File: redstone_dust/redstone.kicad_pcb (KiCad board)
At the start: 2 copper layers, 40 x 40 mm, 73 parts, among them J1 1x4_Pogo, J2 1x4_Pogo, J3 1x4_Pogo, J4 1x4_Pogo, J5 1x4_Pogo, J6 1x4_Pogo, J7 1x4_Pogo, J8 1x4_Pogo, J9 2.54mm_ProgrammingPin, Q1 BC108, Q2 BC108, Q3 BC108, Q4 BC108, SW1 SW_Push_Open, U1 RP2040, U2 RBT05W24S05, U3 TPS62162DSG, U5 W25Q16JVSS

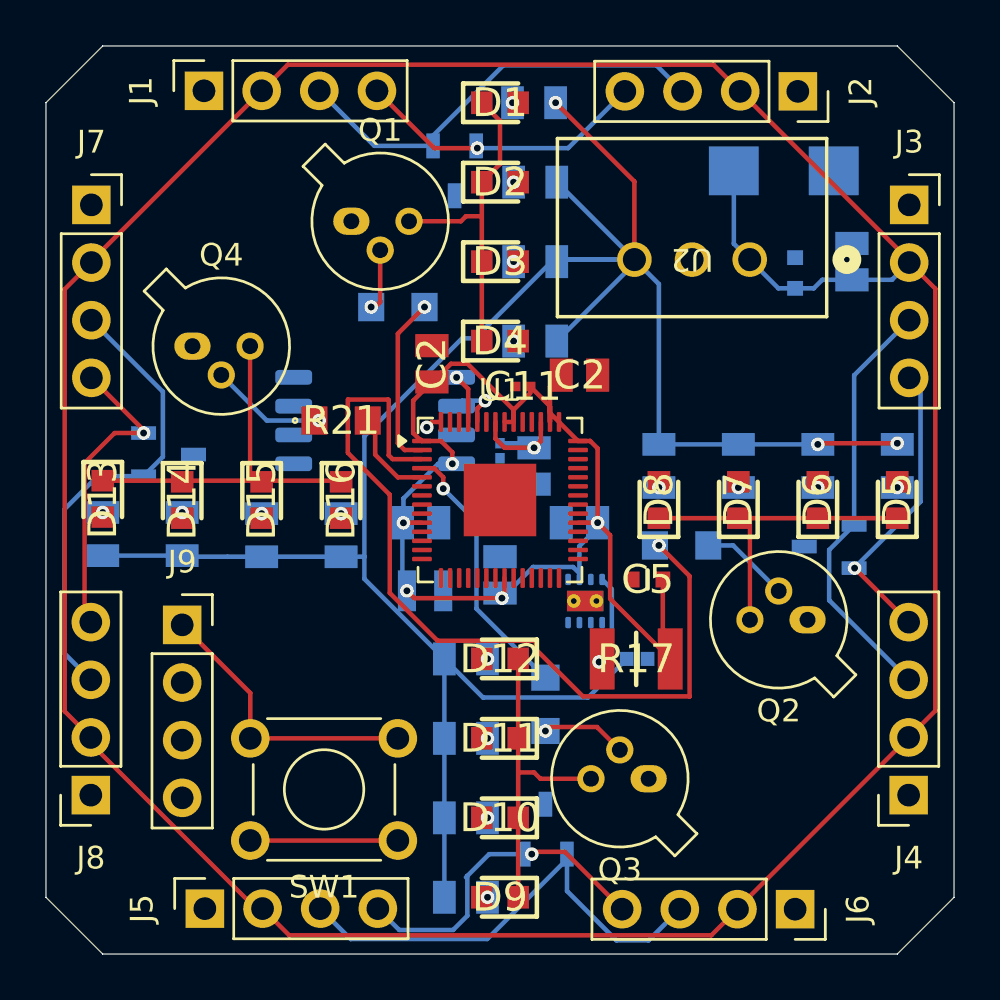
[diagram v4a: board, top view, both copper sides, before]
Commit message: remove all traces to restart layout
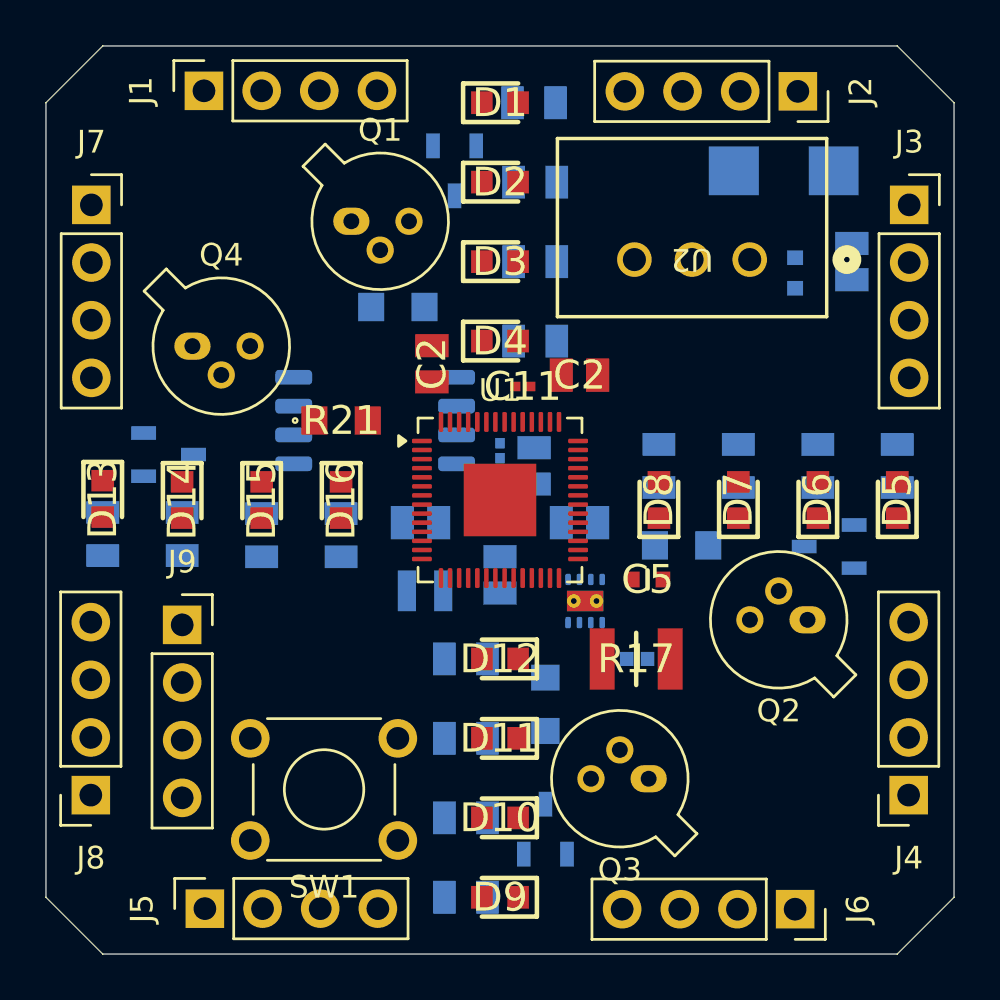
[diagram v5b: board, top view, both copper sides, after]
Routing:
- net VCC: track 142.7 -> 0.00 mm
- net /5V_LOCAL: track 98.8 -> 0.00 mm, vias 3 -> 0
- net /3.3V_LOCAL: track 62.5 -> 0.00 mm, vias 5 -> 0
- net Net-(U1-GPIO1): track 37.8 -> 0.00 mm, vias 1 -> 0
- net /S_TX: track 21.2 -> 0.00 mm
- net /W_TX: track 20.6 -> 0.00 mm
- net /N_TX: track 19.2 -> 0.00 mm
- net /E_TX: track 18.7 -> 0.00 mm
- net Net-(D13-K): track 16.5 -> 0.00 mm
- net Net-(D5-K): track 15.0 -> 0.00 mm
- net Net-(D1-K): track 14.5 -> 0.00 mm
- net /S_RX: track 14.4 -> 0.00 mm, vias 1 -> 0
- net Net-(D10-K): track 13.8 -> 0.00 mm
- net /W_RX: track 13.7 -> 0.00 mm, vias 1 -> 0
- net /E_RX: track 13.3 -> 0.00 mm, vias 1 -> 0
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
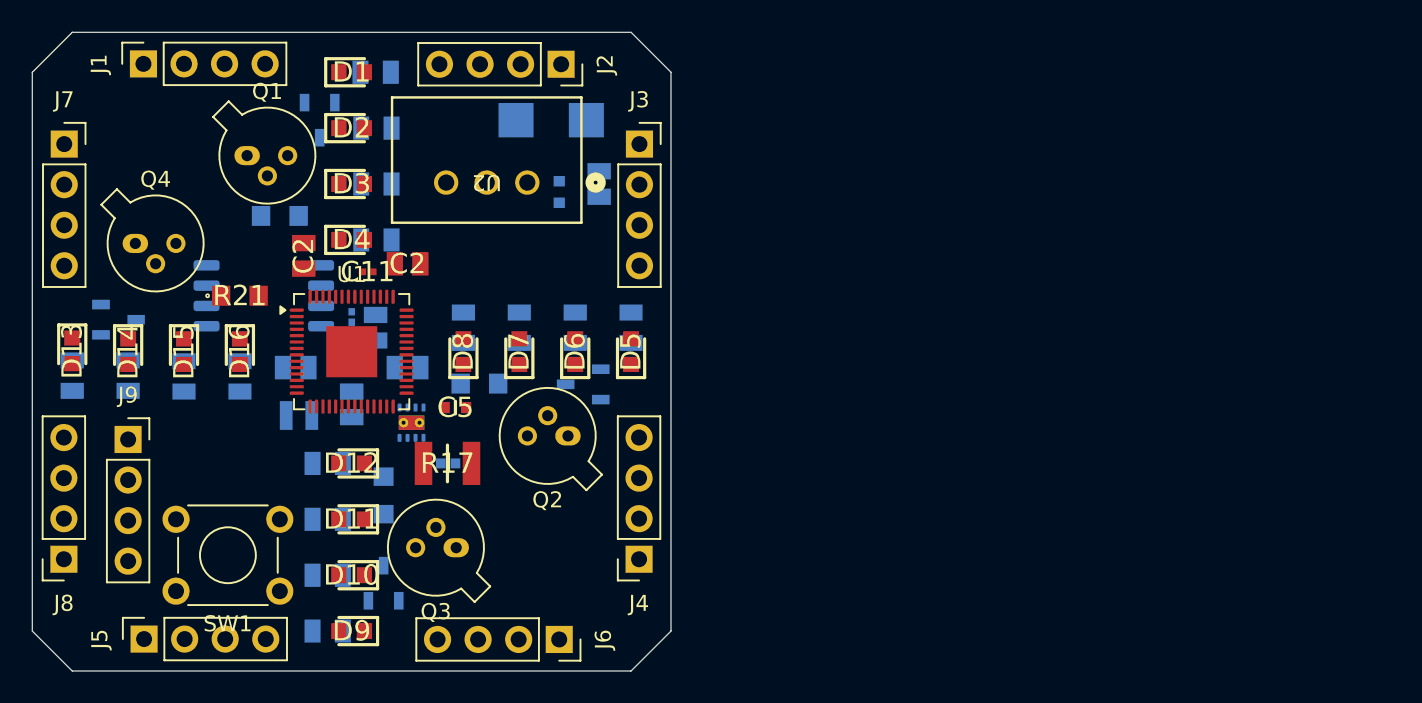
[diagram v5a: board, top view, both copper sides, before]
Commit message: redoing pcb layout with new approach
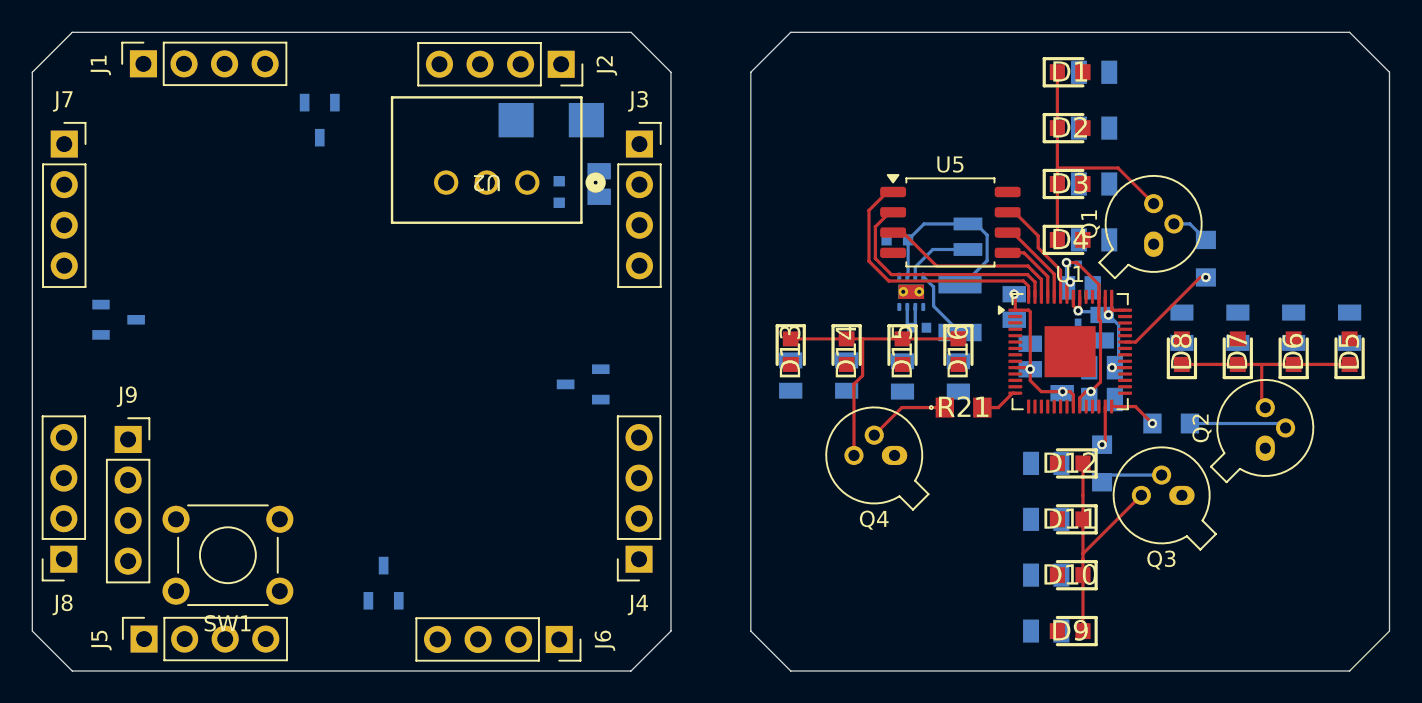
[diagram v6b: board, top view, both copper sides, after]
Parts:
- removed the C10 at (91.5, 53.5)
- removed the C2 at (87.0, 49.0)
- removed the C2 at (93.5, 56.0)
- removed the C2 at (90.0, 58.3)
- removed the C2 at (86.5, 56.0)
- added C10: 0.1uF, SamacSys_Parts:CAPC2012X140N, B.Cu at (135.6, 51.0)
- added C10: 0.1uF, SamacSys_Parts:CAPC2012X140N, B.Cu at (137.0, 58.0)
- added C2: 0.1uF, SamacSys_Parts:CAPC2012X140N, B.Cu at (131.5, 52.2)
- added C2: 0.1uF, SamacSys_Parts:CAPC2012X140N, B.Cu at (134.5, 56.8)
- added C2: 0.1uF, SamacSys_Parts:CAPC2012X140N, B.Cu at (132.5, 55.3)
- added C2: 0.1uF, SamacSys_Parts:CAPC2012X140N, B.Cu at (137.0, 56.0)
- C11, C2, C5, R17: moved to B.Cu
- U2: footprint footprints:RBT10W24S05_XPP_XPR -> SamacSys_Parts:RBT10W24S05_XPP_XPR
- U5: moved to F.Cu
- moved R18 58.1 mm to (143.5, 49.2), turned to -90 degrees
- moved Q1 57.0 mm to (140.2, 48.3), turned to 90 degrees
- moved Q4 49.4 mm to (124.0, 61.5), turned to 180 degrees
- moved R21 45.9 mm to (128.3, 58.5)
- moved Q3 45.6 mm to (142.0, 64.0)
- moved C9 45.3 mm to (135.2, 49.5), turned to 0 degrees
- moved R20 45.0 mm to (137.0, 62.0)
- moved D13 45.0 mm to (117.5, 55.0)
- moved D1 45.0 mm to (135.0, 37.5)
- moved D10 45.0 mm to (135.0, 69.0)
- moved D11 45.0 mm to (135.0, 65.5)
- moved D12 45.0 mm to (135.0, 62.0)
- moved D14 45.0 mm to (121.0, 55.0)
- moved D15 45.0 mm to (124.5, 55.0)
- moved D16 45.0 mm to (128.0, 55.0)
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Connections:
- R18 pad 2: Net-(U1-GPIO0) -> Net-(U1-GPIO25)
- R19 pad 2: Net-(U1-GPIO1) -> Net-(U1-GPIO17)
- R20 pad 2: Net-(U1-GPIO2) -> Net-(U1-GPIO16)
- R21 pad 2: Net-(U1-GPIO3) -> Net-(U1-GPIO11)
- U1 pad 13: /W_RX -> unconnected-(U1-GPIO10-Pad13)
- U1 pad 14: /W_TX -> Net-(U1-GPIO11)
- U1 pad 2: Net-(U1-GPIO0) -> /W_RX
- U1 pad 27: unconnected-(U1-GPIO16-Pad27) -> Net-(U1-GPIO16)
- U1 pad 28: unconnected-(U1-GPIO17-Pad28) -> Net-(U1-GPIO17)
- U1 pad 3: Net-(U1-GPIO1) -> /W_TX
- U1 pad 37: unconnected-(U1-GPIO25-Pad37) -> Net-(U1-GPIO25)
- U1 pad 4: Net-(U1-GPIO2) -> unconnected-(U1-GPIO2-Pad4)
- U1 pad 5: Net-(U1-GPIO3) -> unconnected-(U1-GPIO3-Pad5)
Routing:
- net /3.3V_LOCAL: track 0.00 -> 34.6 mm, vias 0 -> 6
- net Net-(D13-K): track 0.00 -> 18.0 mm
- net Net-(D1-K): track 0.00 -> 17.5 mm
- net Net-(U1-QSPI_SS): track 0.00 -> 17.0 mm
- net Net-(D10-K): track 0.00 -> 15.7 mm
- net Net-(U1-QSPI_SD1): track 0.00 -> 15.0 mm
- net Net-(U1-VREG_VOUT): track 0.00 -> 13.3 mm, vias 0 -> 3
- net Net-(D5-K): track 0.00 -> 13.3 mm
- net Net-(U1-QSPI_SD2): track 0.00 -> 12.2 mm
- net Net-(U1-QSPI_SD3): track 0.00 -> 6.88 mm
- net Net-(U1-GPIO25): track 0.00 -> 6.74 mm, vias 0 -> 1
- net Net-(Q2-B): track 0.00 -> 6.11 mm
- net Net-(U1-QSPI_SCLK): track 0.00 -> 5.37 mm
- net Net-(Q4-B): track 0.00 -> 5.14 mm
- net Net-(U3-PG): track 0.00 -> 4.45 mm
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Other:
- board size 40 x 40 mm -> 85 x 40 mm

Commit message: move pogo pin footprints over to new layout
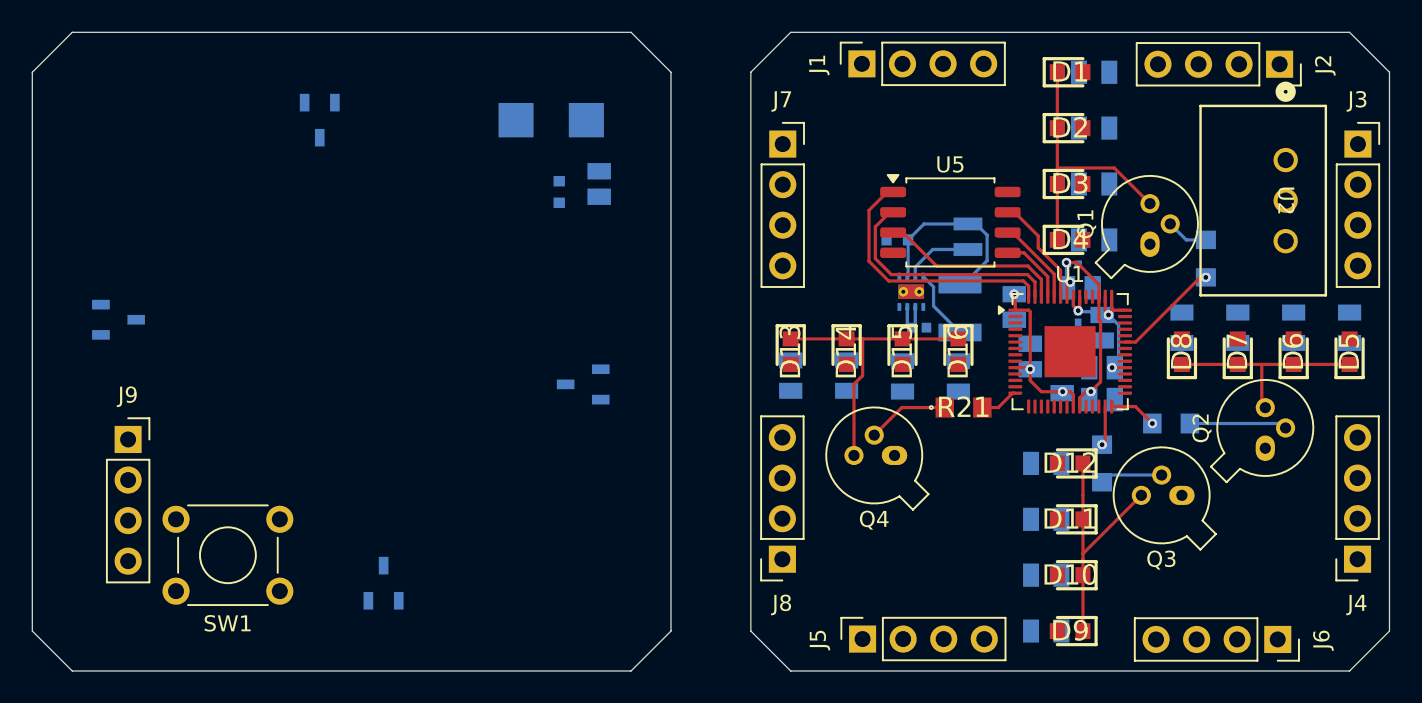
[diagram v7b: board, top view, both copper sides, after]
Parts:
- moved U2 47.5 mm to (148.5, 43.0), turned to -90 degrees
- moved J1 45.0 mm to (122.0, 37.0)
- moved J2 45.0 mm to (148.1, 37.0)
- moved J3 45.0 mm to (153.0, 42.0)
- moved J4 45.0 mm to (153.0, 68.0)
- moved J5 45.0 mm to (122.0, 73.0)
- moved J6 45.0 mm to (148.0, 73.0)
- moved J7 45.0 mm to (117.0, 42.0)
- moved J8 45.0 mm to (117.0, 68.0)
- moved Q1 0.23 mm to (140.0, 48.3)
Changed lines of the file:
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@@
 	(footprint "SamacSys_Parts:RBT10W24S05_XPP_XPR"
 		(layer "F.Cu")
-		(at 101 44.4097 180)
+		(at 148.5 43 -90)
 		(tags "RBT05W24S05 ")
 		(property "Reference" "U2"
-			(at 2.54 0 180)
+			(at 2.54 0 270)
 			(unlocked yes)
 			(layer "F.SilkS")
@@
 		)
 		(property "Value" "RBT05W24S05"
-			(at 2.54 0 180)
+			(at 2.54 0 270)
 			(unlocked yes)
 			(layer "F.Fab")
@@
 		)
 		(property "Datasheet" "RBT05W24S05"
-			(at 0 0 180)
+			(at 0 0 90)
 			(layer "F.Fab")
 			(hide yes)
@@
 		)
 		(property "Description" ""
-			(at 0 0 180)
+			(at 0 0 90)
 			(layer "F.Fab")
 			(hide yes)
@@
 		(attr through_hole)
 		(fp_line
-			(start 8.4709 5.334)
-			(end 8.4709 -2.5146)
+			(start -3.3909 5.334)
+			(end 8.4709 5.334)
 			(stroke
 				(width 0.1524)
@@
 		)
 		(fp_line
-			(start 8.4709 -2.5146)
-			(end -3.3909 -2.5146)
+			(start 8.4709 5.334)
+			(end 8.4709 -2.5146)
 			(stroke
 				(width 0.1524)
@@
 		)
 		(fp_line
-			(start -3.3909 5.334)
-			(end 8.4709 5.334)
+			(start -3.3909 -2.5146)
+			(end -3.3909 5.334)
 			(stroke
 				(width 0.1524)
@@
 		)
 		(fp_line
-			(start -3.3909 -2.5146)
-			(end -3.3909 5.334)
+			(start 8.4709 -2.5146)
+			(end -3.3909 -2.5146)
 			(stroke
 				(width 0.1524)
@@
 		)
 		(fp_line
-			(start 8.5979 5.461)
-			(end 8.5979 -2.6416)
+			(start -3.5179 5.461)
+			(end 8.5979 5.461)
 			(stroke
 				(width 0.1524)
@@
 		)
 		(fp_line
-			(start 8.5979 -2.6416)
-			(end -3.5179 -2.6416)
+			(start 8.5979 5.461)
+			(end 8.5979 -2.6416)
 			(stroke
 				(width 0.1524)
@@
 		)
 		(fp_line
-			(start -3.5179 5.461)
-			(end 8.5979 5.461)
+			(start -3.5179 -2.6416)
+			(end -3.5179 5.461)
 			(stroke
 				(width 0.1524)
@@
 		)
 		(fp_line
-			(start -3.5179 -2.6416)
-			(end -3.5179 5.461)
+			(start 8.5979 -2.6416)
+			(end -3.5179 -2.6416)
 			(stroke
 				(width 0.1524)
@@
 		)
 		(fp_line
-			(start 8.3439 5.207)
-			(end 8.3439 -2.3876)
+			(start -3.2639 5.207)
+			(end 8.3439 5.207)
 			(stroke
 				(width 0.0254)
@@
 		)
 		(fp_line
-			(start 8.3439 -2.3876)
-			(end -3.2639 -2.3876)
+			(start 8.3439 5.207)
+			(end 8.3439 -2.3876)
 			(stroke
 				(width 0.0254)
@@
 		)
 		(fp_line
-			(start -3.2639 5.207)
-			(end 8.3439 5.207)
+			(start -3.2639 -2.3876)
+			(end -3.2639 5.207)
 			(stroke
 				(width 0.0254)
@@
 		)
 		(fp_line
-			(start -3.2639 -2.3876)
-			(end -3.2639 5.207)
+			(start 8.3439 -2.3876)
+			(end -3.2639 -2.3876)
 			(stroke
 				(width 0.0254)
@@
 		)
 		(fp_text user "${REFERENCE}"
-			(at 2.54 0 180)
+			(at 2.54 0 270)
 			(unlocked yes)
 			(layer "F.Fab")
@@
 		)
 		(pad "1" thru_hole circle
-			(at 0 0 180)
+			(at 0 0 270)
 			(size 1.524 1.524)
 			(drill 1.016)
@@
 		)
 		(pad "2" thru_hole circle
-			(at 2.54 0 180)
+			(at 2.54 0 270)
 			(size 1.524 1.524)
 			(drill 1.016)
@@
 		)
 		(pad "3" thru_hole circle
-			(at 5.08 0 180)
+			(at 5.08 0 270)
 			(size 1.524 1.524)
 			(drill 1.016)
@@
 	(footprint "Connector_PinSocket_2.54mm:PinSocket_1x04_P2.54mm_Vertical"
 		(layer "F.Cu")
-		(at 71.975 68 180)
+		(at 116.975 68 180)
 		(descr "Through hole straight socket strip, 1x04, 2.54mm pitch, single row (from Kicad 4.0.7), script generated")
 		(tags "Through hole socket strip THT 1x04 2.54mm single row")
@@
 	(footprint "Connector_PinSocket_2.54mm:PinSocket_1x04_P2.54mm_Vertical"
 		(layer "F.Cu")
-		(at 108 68 180)
+		(at 153 68 180)
 		(descr "Through hole straight socket strip, 1x04, 2.54mm pitch, single row (from Kicad 4.0.7), script generated")
 		(tags "Through hole socket strip THT 1x04 2.54mm single row")
@@
 	(footprint "Connector_PinSocket_2.54mm:PinSocket_1x04_P2.54mm_Vertical"
 		(layer "F.Cu")
-		(at 76.96 36.975 90)
+		(at 121.96 36.975 90)
 		(descr "Through hole straight socket strip, 1x04, 2.54mm pitch, single row (from Kicad 4.0.7), script generated")
 		(tags "Through hole socket strip THT 1x04 2.54mm single row")
@@
 	(footprint "Connector_PinSocket_2.54mm:PinSocket_1x04_P2.54mm_Vertical"
 		(layer "F.Cu")
-		(at 103.12 37 -90)
+		(at 148.12 37 -90)
 		(descr "Through hole straight socket strip, 1x04, 2.54mm pitch, single row (from Kicad 4.0.7), script generated")
 		(tags "Through hole socket strip THT 1x04 2.54mm single row")
@@
 	(footprint "Package_TO_SOT_THT:TO-18-3"
 		(layer "F.Cu")
-		(at 140.23 48.27 90)
+		(at 140 48.27 90)
 		(descr "TO-18-3, generated with kicad-footprint-generator TO_SOT_THT_generate.py")
 		(tags "TO-18-3")
@@
 	(footprint "Connector_PinSocket_2.54mm:PinSocket_1x04_P2.54mm_Vertical"
 		(layer "F.Cu")
-		(at 103 73.025 -90)
+		(at 148 73.025 -90)
 		(descr "Through hole straight socket strip, 1x04, 2.54mm pitch, single row (from Kicad 4.0.7), script generated")
 		(tags "Through hole socket strip THT 1x04 2.54mm single row")
@@
 	(footprint "Connector_PinSocket_2.54mm:PinSocket_1x04_P2.54mm_Vertical"
 		(layer "F.Cu")
-		(at 77 73 90)
+		(at 122 73 90)
 		(descr "Through hole straight socket strip, 1x04, 2.54mm pitch, single row (from Kicad 4.0.7), script generated")
 		(tags "Through hole socket strip THT 1x04 2.54mm single row")
@@
 	(footprint "Connector_PinSocket_2.54mm:PinSocket_1x04_P2.54mm_Vertical"
 		(layer "F.Cu")
-		(at 72 42)
+		(at 117 42)
 		(descr "Through hole straight socket strip, 1x04, 2.54mm pitch, single row (from Kicad 4.0.7), script generated")
 		(tags "Through hole socket strip THT 1x04 2.54mm single row")
@@
 	(footprint "Connector_PinSocket_2.54mm:PinSocket_1x04_P2.54mm_Vertical"
 		(layer "F.Cu")
-		(at 108.025 42)
+		(at 153.025 42)
 		(descr "Through hole straight socket strip, 1x04, 2.54mm pitch, single row (from Kicad 4.0.7), script generated")
 		(tags "Through hole socket strip THT 1x04 2.54mm single row")
@@
 	)
 	(segment
-		(start 134.2 43.5)
-		(end 134.2 37.5)
+		(start 137.77 43.5)
+		(end 140 45.73)
 		(width 0.2)
 		(layer "F.Cu")
@@
 	)
 	(segment
-		(start 138 43.5)
-		(end 140.23 45.73)
+		(start 134.2 43.5)
+		(end 134.2 37.5)
 		(width 0.2)
 		(layer "F.Cu")
@@
 	(segment
 		(start 134.2 43.5)
-		(end 138 43.5)
+		(end 137.77 43.5)
 		(width 0.2)
 		(layer "F.Cu")
@@
 	)
 	(segment
-		(start 141.5 47)
-		(end 142.5 47)
+		(start 142.27 48)
+		(end 141.27 47)
 		(width 0.2)
 		(layer "B.Cu")
@@
 	)
 	(segment
-		(start 142.5 47)
-		(end 143.5 48)
+		(start 143.5 48)
+		(end 142.27 48)
 		(width 0.2)
 		(layer "B.Cu")

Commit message: connect more traces, progress is well
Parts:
- D17: moved to F.Cu
- moved D17 52.0 mm to (139.9, 41.0)
- moved SW1 44.5 mm to (130.0, 70.0)
- moved Q4 1.58 mm to (123.5, 60.0)
- moved R18 0.96 mm to (143.0, 50.0), turned to 180 degrees
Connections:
- R18 pad 2: Net-(U1-GPIO25) -> Net-(U1-GPIO23)
- U1 pad 31: unconnected-(U1-GPIO20-Pad31) -> /E_RX
- U1 pad 32: unconnected-(U1-GPIO21-Pad32) -> /E_TX
- U1 pad 35: unconnected-(U1-GPIO23-Pad35) -> Net-(U1-GPIO23)
- U1 pad 36: unconnected-(U1-GPIO24-Pad36) -> /N_RX
- U1 pad 37: Net-(U1-GPIO25) -> /N_TX
- U1 pad 6: /N_RX -> unconnected-(U1-GPIO4-Pad6)
- U1 pad 7: /N_TX -> unconnected-(U1-GPIO5-Pad7)
- U1 pad 8: /E_RX -> unconnected-(U1-GPIO6-Pad8)
- U1 pad 9: /E_TX -> unconnected-(U1-GPIO7-Pad9)
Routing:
- net /5V_LOCAL: track 2.81 -> 49.1 mm
- net /N_TX: track 0.00 -> 30.2 mm
- net /N_RX: track 0.00 -> 23.6 mm
- net /E_TX: track 0.00 -> 13.3 mm
- net /E_RX: track 0.00 -> 12.4 mm
- net /W_TX: track 0.00 -> 11.6 mm
- net /W_RX: track 0.00 -> 10.9 mm
- net /3.3V_LOCAL: track 34.6 -> 43.5 mm
- net VCC: track 0.00 -> 7.21 mm
- net Net-(U1-GPIO23): track 0.00 -> 7.19 mm, vias 0 -> 1
- net Net-(U1-GPIO25): track 6.74 -> 0.00 mm, vias 1 -> 0
- net Net-(Q1-B): track 2.64 -> 4.20 mm
- net Net-(D13-K): track 18.0 -> 16.7 mm
- net Net-(D1-A): track 0.00 -> 0.55 mm, vias 0 -> 1
- net Net-(D14-A): track 0.00 -> 0.55 mm, vias 0 -> 1
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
